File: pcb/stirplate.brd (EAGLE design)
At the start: 79.7 x 35.5 mm, 18 parts, among them IC1 ATMEGA168-PU, IC2 7805T, T1 2N2222, X1 HD44780LCD-1602

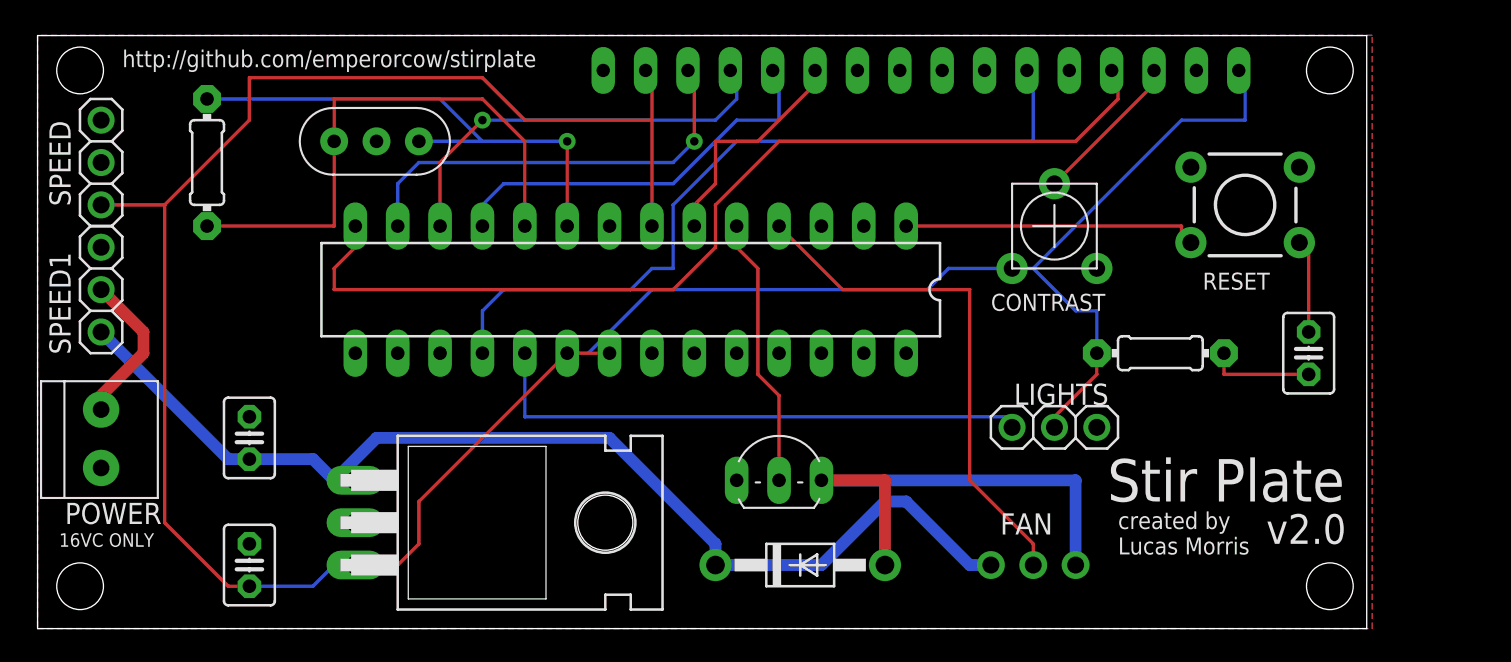
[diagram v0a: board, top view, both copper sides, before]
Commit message: Fixed a few issues on the new eagle board
Upgraded LCD to an Adafruit RGB, fixed some routing caused by that.
Moved header for radial pot to a 1x5 screw terminal and fixed routing on
that.
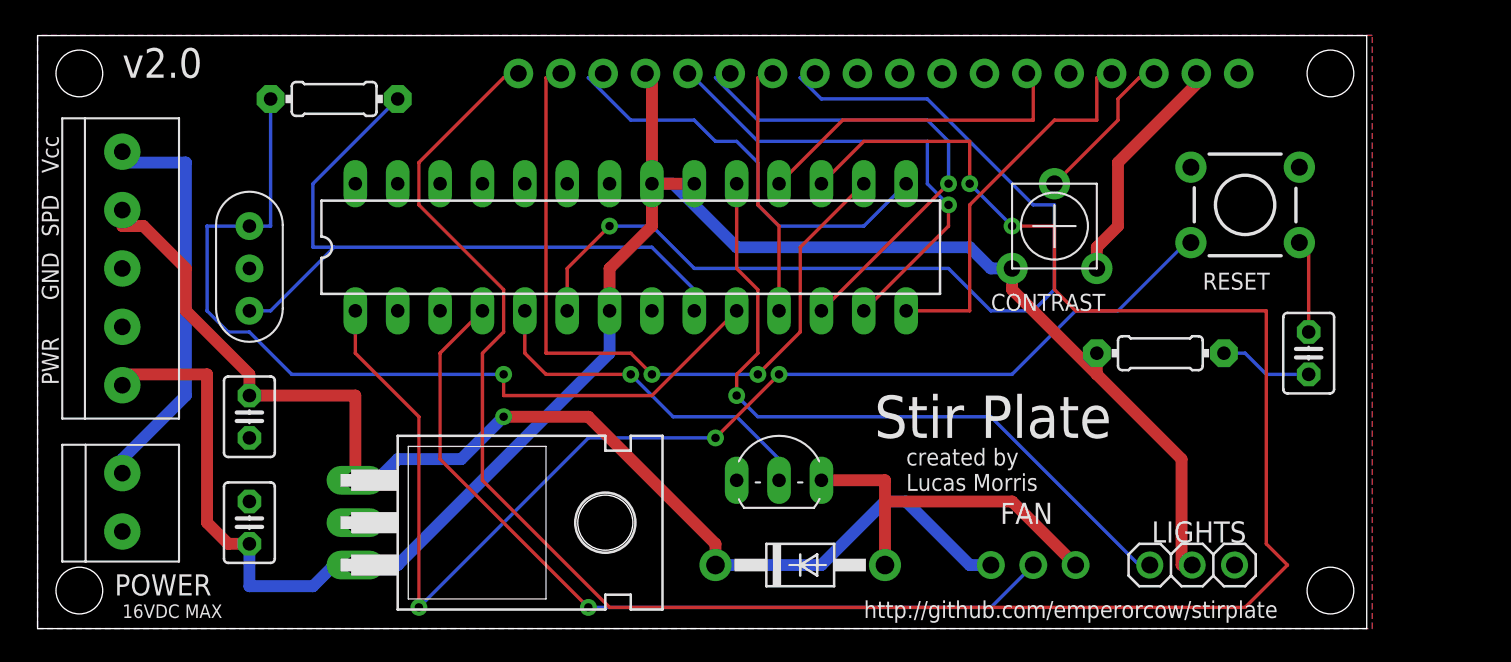
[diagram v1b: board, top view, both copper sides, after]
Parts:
- removed SPEED1: (no value), adafruit:1X03
- removed X1: HD44780LCD-1602, adafruit:LCD1602
- added U$1: HD44780LCD_RGBLONGPINS, adafruit:LCD1602-RGB
- SPEED: value (none) -> 1X5; device adafruit:1X03 -> adafruit:1X05-3.5MM
- moved LIGHTS 11.7 mm to (69.2, 3.81)
- moved CLOCK 10.8 mm to (12.7, 21.6), turned to 90 degrees
- moved R2 8.52 mm to (17.8, 31.8), turned to 0 degrees
- moved SPEED 6.48 mm to (5.08, 21.6), turned to 270 degrees
- moved POWER 4.02 mm to (5.08, 7.62)
- moved C3 2.54 mm to (12.7, 6.35)
- moved IC1 2.54 mm to (35.6, 22.9), turned to 0 degrees
- moved C2 1.27 mm to (12.7, 12.7), turned to 270 degrees
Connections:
- new net VDD: CONTRAST.3, U$1.2
- new net VSS: U$1.1
- net +5V: now also U$1.15; no longer X1.1, X1.15
- net BLUE: now also U$1.18
- net GND: now also U$1.5; no longer CONTRAST.3, X1.16, X1.2, X1.5
- net GREEN: now also U$1.17
- net LCD_DB4: now also U$1.11; no longer X1.11
- net LCD_DB5: now also U$1.12; no longer X1.12
- net LCD_DB6: now also U$1.13; no longer X1.13
- net LCD_DB7: now also U$1.14; no longer X1.14
- net LCD_E: now also U$1.6; no longer X1.6
- net LCD_RS: now also U$1.4; no longer X1.4
- net N$7: now also U$1.3; no longer X1.3
- net RED: now also U$1.16
- net SRC-VCC: now also SPEED.5; no longer SPEED1.2
- net VCC: now also SPEED.4; no longer SPEED1.1
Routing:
- net BLUE: track 0.00 -> 133.7 mm, vias 0 -> 2
- net N$4: track 18.4 -> 74.6 mm, vias 0 -> 3
- net +5V: track 165.2 -> 115.8 mm
- net LCD_DB4: track 14.1 -> 59.8 mm, vias 0 -> 1
- net GREEN: track 0.00 -> 44.7 mm, vias 0 -> 2
- net LCD_RS: track 59.4 -> 23.3 mm
- net LCD_E: track 46.4 -> 19.8 mm
- net RED: track 0.00 -> 26.2 mm
- net N$2: track 32.8 -> 53.2 mm, vias 0 -> 1
- net HALL: track 31.1 -> 50.2 mm, vias 0 -> 1
- net SRC-VCC: track 9.29 -> 24.7 mm
- net VDD: track 0.00 -> 14.5 mm
- net N$1: track 31.5 -> 42.8 mm, vias 1 -> 0
- net NEOPIXEL: track 33.7 -> 42.7 mm, vias 0 -> 1
- net LCD_DB5: track 24.3 -> 15.4 mm
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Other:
- board text added: "16VDC MAX"
- board text added: "GND"
- board text added: "PWR"
- board text added: "SPD"
- board text added: "Vcc"
- board text removed: "16VC ONLY"
